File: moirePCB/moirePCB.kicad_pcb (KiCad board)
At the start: 4 copper layers, 30 x 228.8 mm, 37 parts, among them J1 USB_C_Receptacle, J2 Conn_01x12_Pin, SW3 SW_DPDT_x2, U1 ESP32-PICO-D4, U2 BQ24075RGT, U3 TLV73333PDBV, U4 RFM95W-915S2, U5 CH340E, U6 TLC555xD, U7 HDC1080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

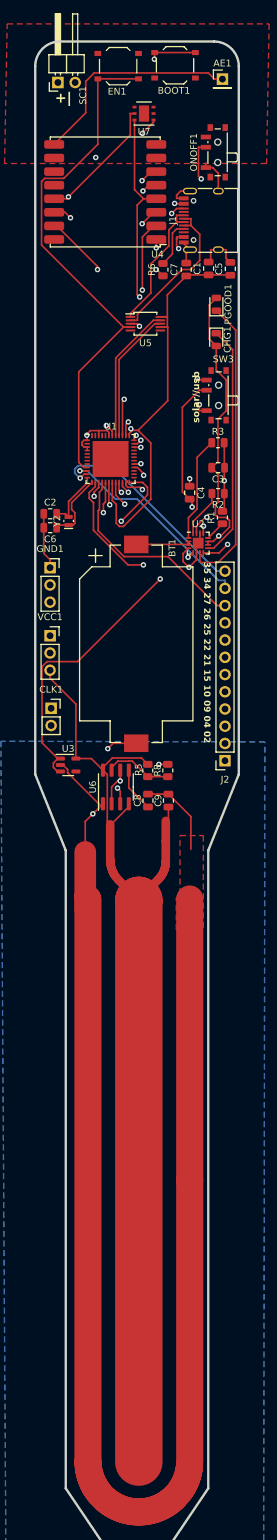
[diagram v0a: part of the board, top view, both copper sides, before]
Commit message: pins and jumpers, transistor A_RAIL
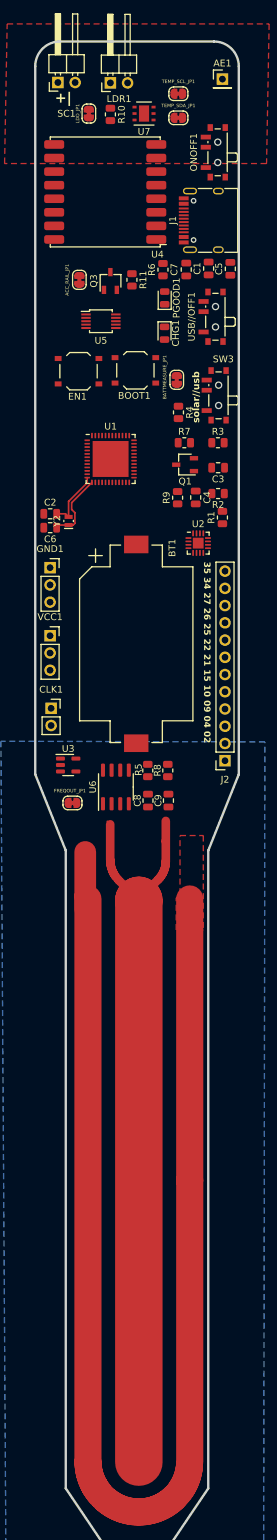
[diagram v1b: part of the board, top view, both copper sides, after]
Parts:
- added ACC_RAIL_JP1: SolderJumper_2_Bridged, Jumper:SolderJumper-2_P1.3mm_Bridged_RoundedPad1.0x1.5mm, F.Cu at (46.5, 46.9)
- added BATTMEASURE_JP1: SolderJumper_2_Bridged, Jumper:SolderJumper-2_P1.3mm_Bridged_RoundedPad1.0x1.5mm, F.Cu at (60.8, 61.6)
- added FREQOUT_JP1: SolderJumper_2_Bridged, Jumper:SolderJumper-2_P1.3mm_Bridged_RoundedPad1.0x1.5mm, F.Cu at (45.5, 124.0)
- added LDO_JP1: SolderJumper_2_Bridged, Jumper:SolderJumper-2_P1.3mm_Bridged_RoundedPad1.0x1.5mm, F.Cu at (47.9, 22.4)
- added LDR1: R_Photo 50k-100k, Connector_PinHeader_2.54mm:PinHeader_1x02_P2.54mm_Horizontal, F.Cu at (51.0, 17.8)
- added Q1: NPN, Package_TO_SOT_SMD:TSOT-23, F.Cu at (62.1, 74.1)
- added Q3: NPN, Package_TO_SOT_SMD:TSOT-23, F.Cu at (51.1, 47.0)
- added R10: 360k, Resistor_SMD:R_0805_2012Metric, F.Cu at (51.1, 22.5)
- added R11: 10k, Resistor_SMD:R_0805_2012Metric, F.Cu at (54.2, 46.9)
- added R4: 270k, Resistor_SMD:R_0805_2012Metric, F.Cu at (61.1, 66.4)
- added R7: 820k, Resistor_SMD:R_0805_2012Metric, F.Cu at (62.0, 70.9)
- added R9: 10k, Resistor_SMD:R_0805_2012Metric, F.Cu at (61.0, 79.0)
- added TEMP_SCL_JP1: SolderJumper_2_Bridged, Jumper:SolderJumper-2_P1.3mm_Bridged_RoundedPad1.0x1.5mm, F.Cu at (61.1, 19.4)
- added TEMP_SDA_JP1: SolderJumper_2_Bridged, Jumper:SolderJumper-2_P1.3mm_Bridged_RoundedPad1.0x1.5mm, F.Cu at (61.1, 23.0)
- added USB//OFF1: SW_DPDT_x2, Button_Switch_SMD:SW_SPDT_PCM12, F.Cu at (66.2, 52.3)
- moved BOOT1 45.3 mm to (54.7, 60.2)
- moved EN1 45.3 mm to (46.4, 60.3)
- moved CHG1 7.68 mm to (59.0, 54.7)
- moved PGOOD1 7.68 mm to (59.1, 49.5)
- moved U5 6.57 mm to (49.7, 53.0)
- moved C4 1.13 mm to (63.6, 78.9)
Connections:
- net /GPIO_25 renamed BATT_MEASURE
- C7 pad 1: VCC -> Net-(U5-V3)
- C9 pad 1: VCC -> A_VCC
- CLK1 pad 1: /GPIO_18 -> /GPIO_22
- J2 pad 11: /GPIO_34 -> FREQOUT
- R5 pad 2: VCC -> A_VCC
- U1 pad 10: /GPIO_34 -> FREQOUT
- U1 pad 15: FREQOUT -> ACCESSORY_SW
- U5 pad 10: VCC -> Net-(U5-V3)
- U5 pad 7: VCC -> Net-(U5-V3)
- U6 pad 3: FREQOUT -> Net-(FREQOUT_JP1-B)
- U6 pad 4: VCC -> A_VCC
- U6 pad 8: VCC -> A_VCC
- U7 pad 1: /GPIO_22 -> Net-(TEMP_SDA_JP1-A)
- U7 pad 5: VCC -> A_VCC
- U7 pad 6: /GPIO_18 -> Net-(TEMP_SCL_JP1-A)
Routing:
- net VCC: track 320.7 -> 110.1 mm, vias 3 -> 0
- net /GPIO_18: track 99.4 -> 0.00 mm, vias 2 -> 0
- net Net-(CHG1-A): track 95.6 -> 0.00 mm, vias 3 -> 0
- net GND: track 337.5 -> 247.1 mm, vias 9 -> 0
- net /EN: track 77.9 -> 0.00 mm
- net Net-(U1-IO0): track 74.7 -> 0.00 mm, vias 2 -> 0
- net Net-(SC1-+): track 62.2 -> 0.00 mm, vias 1 -> 0
- net /GPIO_14: track 59.6 -> 0.00 mm, vias 2 -> 0
- net Net-(ONOFF1A-B): track 59.3 -> 0.00 mm, vias 2 -> 0
- net /GPIO_13: track 52.0 -> 0.00 mm, vias 2 -> 0
- net FREQOUT: track 49.2 -> 0.00 mm, vias 2 -> 0
- net /GPIO_4: track 48.9 -> 0.00 mm, vias 1 -> 0
- net /GPIO_2: track 48.9 -> 0.00 mm, vias 1 -> 0
- net /GPIO_22: track 48.4 -> 0.00 mm, vias 2 -> 0
- net /GPIO_12: track 48.3 -> 0.00 mm, vias 2 -> 0
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
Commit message: pcb 2 final (submitted to jlc)
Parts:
- removed Q1, Q3: NPN, Package_TO_SOT_SMD:TSOT-23
- added EN2_JP1: SolderJumper_2_Bridged, Jumper:SolderJumper-2_P1.3mm_Bridged_RoundedPad1.0x1.5mm, F.Cu at (66.0, 90.9)
- added U8: AP2281-1WG-7, Package_TO_SOT_SMD:SOT-23-6, F.Cu at (62.0, 74.8)
- added U9: AP2281-1WG-7, Package_TO_SOT_SMD:SOT-23-6, F.Cu at (42.9, 67.0)
- J2: value Conn_01x12_Pin -> Conn_01x06_Socket; footprint Connector_PinSocket_2.54mm:PinSocket_1x12_P2.54mm_Vertical -> Connector_PinSocket_2.54mm:PinSocket_1x06_P2.54mm_Vertical
- R1: value 1.18k -> 7.5k
- R11, R9: value 10k -> 1k
- R2: value 1.13k -> 8.2
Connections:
- BT1 pad 1: Net-(BT1-+) -> VCC
- C3 pad 2: Net-(CHG1-A) -> Net-(U3-EN)
- J2 pad 6: /GPIO_21 -> /GPIO_27
- PGOOD1 pad 2: Net-(CHG1-A) -> Net-(PGOOD1-A)
- R11 pad 1: Net-(Q3-B) -> Net-(U3-EN)
- R11 pad 2: ACCESSORY_SW -> Net-(PGOOD1-A)
- R9 pad 1: Net-(Q1-B) -> Net-(U3-EN)
- R9 pad 2: ACCESSORY_SW -> Net-(CHG1-A)
- U1 pad 11: /GPIO_35 -> LDR_MEASURE
- U2 pad 10: Net-(CHG1-A) -> Net-(U3-EN)
- U2 pad 11: Net-(CHG1-A) -> Net-(U3-EN)
- U2 pad 2: Net-(BT1-+) -> VCC
- U2 pad 3: Net-(BT1-+) -> VCC
- U2 pad 5: Net-(CHG1-A) -> Net-(EN2_JP1-B)
- U3 pad 1: Net-(CHG1-A) -> Net-(U3-EN)
- U3 pad 3: Net-(CHG1-A) -> Net-(U3-EN)
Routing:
- net VCC: track 110.1 -> 342.9 mm, vias 0 -> 6
- net GND: track 247.1 -> 372.7 mm, vias 0 -> 22
- net A_VCC: track 0.00 -> 125.0 mm, vias 0 -> 2
- net Net-(U3-EN): track 0.00 -> 116.1 mm, vias 0 -> 5
- net /GPIO_22: track 0.00 -> 107.8 mm, vias 0 -> 3
- net /GPIO_18: track 0.00 -> 91.5 mm, vias 0 -> 2
- net Net-(SC1-+): track 0.00 -> 68.9 mm, vias 0 -> 1
- net /GPIO_14: track 0.00 -> 63.7 mm, vias 0 -> 2
- net Net-(ONOFF1A-B): track 0.00 -> 61.9 mm, vias 0 -> 2
- net /GPIO_13: track 0.00 -> 59.8 mm, vias 0 -> 2
- net LDR_MEASURE: track 0.00 -> 55.9 mm, vias 0 -> 2
- net FREQOUT: track 0.00 -> 54.8 mm
- net /GPIO_21: track 0.00 -> 53.3 mm, vias 0 -> 2
- net /GPIO_12: track 0.00 -> 49.2 mm, vias 0 -> 2
- net /GPIO_2: track 0.00 -> 47.9 mm, vias 0 -> 2
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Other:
- board text added: "2 4 9 10 15 27"
- board text removed: "35 34 27 26 25 22 21 15 10 09 04 02"

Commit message: initial pcb 3 layout
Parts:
- added C3: .01uF, Capacitor_SMD:C_0805_2012Metric, F.Cu at (57.8, 101.4)
- added C_FLTR1: .1uF, Capacitor_SMD:C_0805_2012Metric, F.Cu at (57.8, 104.4)
- added C_HVR1: 4.7uF, Capacitor_SMD:C_0805_2012Metric, F.Cu at (57.8, 107.4)
- added C_STOR1: 4.7uF, Capacitor_SMD:C_0805_2012Metric, F.Cu at (57.8, 110.4)
- added L_BST1: 22uH, Inductor_SMD:L_0805_2012Metric, F.Cu at (61.2, 97.7)
- added R_OC_1: R, Resistor_SMD:R_0805_2012Metric, F.Cu at (47.9, 92.5)
- added R_OC_2: R, Resistor_SMD:R_0805_2012Metric, F.Cu at (47.9, 95.4)
- added R_OK_1: R, Resistor_SMD:R_0805_2012Metric, F.Cu at (47.9, 98.4)
- added R_OK_2: R, Resistor_SMD:R_0805_2012Metric, F.Cu at (52.3, 92.5)
- added R_OK_3: R, Resistor_SMD:R_0805_2012Metric, F.Cu at (52.3, 95.4)
- added R_OV_1: R, Resistor_SMD:R_0805_2012Metric, F.Cu at (52.3, 98.4)
- added R_OV_2: R, Resistor_SMD:R_0805_2012Metric, F.Cu at (56.8, 92.5)
- added R_UV_1: R, Resistor_SMD:R_0805_2012Metric, F.Cu at (56.8, 95.4)
- added R_UV_2: R, Resistor_SMD:R_0805_2012Metric, F.Cu at (56.8, 98.4)
- added U10: TLV73333PDBV, Package_TO_SOT_SMD:SOT-23-5, F.Cu at (62.6, 106.5)
- added U2: BQ25504, Package_DFN_QFN:VQFN-16-1EP_3x3mm_P0.5mm_EP1.68x1.68mm, F.Cu at (61.6, 93.7)
- added U3: TLV73333PDBV, Package_TO_SOT_SMD:SOT-23-5, F.Cu at (62.6, 102.1)
- added USB//SOLAR1: SW_DPDT_x2, Button_Switch_SMD:SW_SPDT_PCM12, F.Cu at (50.6, 102.8)
- BT1: footprint Battery:BatteryHolder_Keystone_1060_1x2032 -> Connector_JST:JST_EH_S2B-EH_1x02_P2.50mm_Horizontal
- moved BT1 11.9 mm to (47.6, 110.0)
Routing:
- net VCC: track 342.9 -> 110.1 mm, vias 6 -> 0
- net GND: track 372.7 -> 247.1 mm, vias 22 -> 0
- net A_VCC: track 125.0 -> 0.00 mm, vias 2 -> 0
- net Net-(U3-EN): track 116.1 -> 0.00 mm, vias 5 -> 0
- net /GPIO_22: track 107.8 -> 0.00 mm, vias 3 -> 0
- net /GPIO_18: track 91.5 -> 0.00 mm, vias 2 -> 0
- net Net-(SC1-+): track 68.9 -> 0.00 mm, vias 1 -> 0
- net /GPIO_14: track 63.7 -> 0.00 mm, vias 2 -> 0
- net Net-(ONOFF1A-B): track 61.9 -> 0.00 mm, vias 2 -> 0
- net /GPIO_13: track 59.8 -> 0.00 mm, vias 2 -> 0
- net LDR_MEASURE: track 55.9 -> 0.00 mm, vias 2 -> 0
- net FREQOUT: track 54.8 -> 0.00 mm
- net /GPIO_21: track 53.3 -> 0.00 mm, vias 2 -> 0
- net /GPIO_12: track 49.2 -> 0.00 mm, vias 2 -> 0
- net /GPIO_2: track 47.9 -> 0.00 mm, vias 2 -> 0
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
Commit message: r values needed
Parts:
- moved U9 21.9 mm to (56.4, 84.3)
- moved USB//SOLAR1 17.9 mm to (67.7, 97.7), turned to 90 degrees
- moved R6 12.6 mm to (61.0, 57.8), turned to 180 degrees
- moved ACC_RAIL_JP1 12.4 mm to (56.3, 54.5)
- moved LDO_JP1 12.3 mm to (57.5, 14.7)
- moved U7 9.40 mm to (61.3, 14.6)
- moved R10 8.38 mm to (59.3, 21.0)
- moved LDR1 6.90 mm to (50.8, 24.7)
- moved SC1 6.90 mm to (43.1, 24.7)
- moved TEMP_SDA_JP1 6.28 mm to (67.1, 21.1), turned to 90 degrees
- moved R11 4.08 mm to (56.3, 50.4)
- moved C3 3.05 mm to (57.4, 104.4)
- moved C_FLTR1 3.05 mm to (57.4, 107.4)
- moved C_HVR1 3.05 mm to (57.4, 110.4)
- moved C_STOR1 3.05 mm to (57.4, 113.4)
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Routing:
- net VCC: track 110.1 -> 0.00 mm
- net FREQOUT: track 0.00 -> 110.1 mm

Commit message: pre route
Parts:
- removed the C3 at (66.9, 74.5)
- removed C4: 1u, Capacitor_SMD:C_0805_2012Metric
- removed CHG1, PGOOD1: LED, LED_SMD:LED_0805_2012Metric
- removed R1: 7.5k, Resistor_SMD:R_0805_2012Metric
- removed R11, R9: 1k, Resistor_SMD:R_0805_2012Metric
- removed R2: 8.2, Resistor_SMD:R_0805_2012Metric
- removed R3: 10k, Resistor_SMD:R_0805_2012Metric
- removed the U2 at (64.0, 85.7)
- added VBAT_OK1: SolderJumper_2_Bridged, Jumper:SolderJumper-2_P1.3mm_Bridged_RoundedPad1.0x1.5mm, F.Cu at (62.2, 91.1)
- moved ACC_RAIL_JP1 26.1 mm to (66.7, 78.3), turned to 0 degrees
- moved R6 23.3 mm to (62.3, 81.0), turned to 0 degrees
- moved BATTMEASURE_JP1 21.1 mm to (66.7, 81.9), turned to 0 degrees
- moved U9 15.9 mm to (66.7, 72.1)
- moved BT1 15.2 mm to (48.6, 95.6)
- moved R_OC_1 14.8 mm to (48.1, 107.2)
- moved R_OC_2 14.8 mm to (48.1, 110.2)
- moved R_OK_1 14.8 mm to (48.1, 113.2)
- moved R_OK_2 14.8 mm to (52.5, 107.2)
- moved R_OK_3 14.8 mm to (52.5, 110.2)
- moved R_OV_1 14.8 mm to (52.5, 113.2)
- moved U2 14.2 mm to (49.8, 101.5)
- moved R7 13.1 mm to (62.3, 84.0)
- moved U8 11.9 mm to (66.6, 85.8)
- moved R4 11.7 mm to (62.3, 78.0), turned to 0 degrees
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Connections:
- BT1 pad 1: VCC -> Net-(BT1-+)
- U10 pad 3: VBAT_OK -> Net-(U10-EN)
- U2 pad 14: VCC -> Net-(BT1-+)
- U8 pad 4: VCC -> Net-(BT1-+)
- U8 pad 6: VCC -> Net-(BT1-+)

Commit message: resistorValues
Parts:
- added R_OC+10: 10M, Resistor_SMD:R_0805_2012Metric, F.Cu at (61.8, 113.5)
- R_OC_1: value R -> 5.76M
- R_OC_2: value R -> 4.12M
- R_OK_1: value R -> 3.57M
- R_OK_2, R_UV_2: value R -> 6.19M
- R_OK_3: value R -> .143M
- R_OV_1: value R -> 4.42M
- R_OV_2: value R -> 5.36M
- R_UV_1: value R -> 3.74M
- moved U3 0.37 mm to (62.2, 105.0)
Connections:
- L_BST1 pad 1: Net-(SC1-+) -> Net-(U2-VIN_DC)
- R_OC_2 pad 2: Net-(U2-VOC_SAMP) -> Net-(R_OC+10-Pad1)
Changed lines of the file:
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@@
   (net 94 "Net-(BT1-+)")
   (net 95 "Net-(U10-EN)")
+  (net 96 "Net-(R_OC+10-Pad1)")
   (footprint "Connector_PinSocket_2.54mm:PinSocket_1x06_P2.54mm_Vertical" (layer "F.Cu")
     (at 67.945 117.729 180)
@@
       (stroke (width 0.1) (type solid)) (layer "F.Fab"))
     (pad "1" smd roundrect (at -1.0625 0) (size 0.875 1.2) (layers "F.Cu" "F.Paste" "F.Mask") (roundrect_rratio 0.25)
-      (net 40 "Net-(SC1-+)") (pinfunction "1") (pintype "passive"))
+      (net 85 "Net-(U2-VIN_DC)") (pinfunction "1") (pintype "passive"))
     (pad "2" smd roundrect (at 1.0625 0) (size 0.875 1.2) (layers "F.Cu" "F.Paste" "F.Mask") (roundrect_rratio 0.25)
       (net 83 "Net-(U2-LBST)") (pinfunction "2") (pintype "passive"))
@@
         (effects (font (size 1 1) (thickness 0.15)))
     )
-    (fp_text value "R" (at 0 1.65) (layer "F.Fab")
+    (fp_text value "6.19M" (at 0 1.65) (layer "F.Fab")
         (effects (font (size 1 1) (thickness 0.15)))
     )
@@
         (effects (font (size 1 1) (thickness 0.15)))
     )
-    (fp_text value "R" (at 0 1.65) (layer "F.Fab")
+    (fp_text value "3.57M" (at 0 1.65) (layer "F.Fab")
         (effects (font (size 1 1) (thickness 0.15)))
     )
@@
         (effects (font (size 1 1) (thickness 0.15)))
     )
-    (fp_text value "R" (at 0 1.65) (layer "F.Fab")
+    (fp_text value "5.36M" (at 0 1.65) (layer "F.Fab")
         (effects (font (size 1 1) (thickness 0.15)))
     )
@@
         (effects (font (size 1 1) (thickness 0.15)))
     )
-    (fp_text value "R" (at 0 1.65) (layer "F.Fab")
+    (fp_text value "4.42M" (at 0 1.65) (layer "F.Fab")
         (effects (font (size 1 1) (thickness 0.15)))
     )
@@
         (effects (font (size 1 1) (thickness 0.15)))
     )
-    (fp_text value "R" (at 0 1.65) (layer "F.Fab")
+    (fp_text value "5.76M" (at 0 1.65) (layer "F.Fab")
         (effects (font (size 1 1) (thickness 0.15)))
     )
@@
   )
   (footprint "Package_TO_SOT_SMD:SOT-23-5" (layer "F.Cu")
-    (at 61.834 105.005)
+    (at 62.2 105.005)
     (descr "SOT, 5 Pin (https://www.jedec.org/sites/default/files/docs/Mo-178c.PDF variant AA), generated with kicad-footprint-generator ipc_gullwing_generator.py")
     (tags "SOT TO_SOT_SMD")
@@
       ))
   )
+  (footprint "Resistor_SMD:R_0805_2012Metric" (layer "F.Cu")
+    (at 61.8125 113.45 180)
+    (descr "Resistor SMD 0805 (2012 Metric), square (rectangular) end terminal, IPC_7351 nominal, (Body size source: IPC-SM-782 page 72, https://www.pcb-3d.com/wordpress/wp-content/uploads/ipc-sm-782a_amendment_1_and_2.pdf), generated with kicad-footprint-generator")
+    (tags "resistor")
+    (property "Sheetfile" "moirePCB.kicad_sch")
+    (property "Sheetname" "")
+    (property "ki_description" "Resistor")
+    (property "ki_keywords" "R res resistor")
+    (attr smd)
+    (fp_text reference "R_OC+10" (at 0 -1.65) (layer "F.SilkS")
+        (effects (font (size 1 1) (thickness 0.15)))
+    )
+    (fp_text value "10M" (at 0 1.65) (layer "F.Fab")
+        (effects (font (size 1 1) (thickness 0.15)))
+    )
+    (fp_text user "${REFERENCE}" (at 0 0) (layer "F.Fab")
+        (effects (font (size 0.5 0.5) (thickness 0.08)))
+    )
+    (fp_line (start -0.227064 -0.735) (end 0.227064 -0.735)
+      (stroke (width 0.12) (type solid)) (layer "F.SilkS"))
+    (fp_line (start -0.227064 0.735) (end 0.227064 0.735)
+      (stroke (width 0.12) (type solid)) (layer "F.SilkS"))
+    (fp_line (start -1.68 -0.95) (end 1.68 -0.95)
+      (stroke (width 0.05) (type solid)) (layer "F.CrtYd"))
+    (fp_line (start -1.68 0.95) (end -1.68 -0.95)
+      (stroke (width 0.05) (type solid)) (layer "F.CrtYd"))
+    (fp_line (start 1.68 -0.95) (end 1.68 0.95)
+      (stroke (width 0.05) (type solid)) (layer "F.CrtYd"))
+    (fp_line (start 1.68 0.95) (end -1.68 0.95)
+      (stroke (width 0.05) (type solid)) (layer "F.CrtYd"))
+    (fp_line (start -1 -0.625) (end 1 -0.625)
+      (stroke (width 0.1) (type solid)) (layer "F.Fab"))
+    (fp_line (start -1 0.625) (end -1 -0.625)
+      (stroke (width 0.1) (type solid)) (layer "F.Fab"))
+    (fp_line (start 1 -0.625) (end 1 0.625)
+      (stroke (width 0.1) (type solid)) (layer "F.Fab"))
+    (fp_line (start 1 0.625) (end -1 0.625)
+      (stroke (width 0.1) (type solid)) (layer "F.Fab"))
+    (pad "1" smd roundrect (at -0.9125 0 180) (size 1.025 1.4) (layers "F.Cu" "F.Paste" "F.Mask") (roundrect_rratio 0.243902)
+      (net 96 "Net-(R_OC+10-Pad1)") (pintype "passive"))
+    (pad "2" smd roundrect (at 0.9125 0 180) (size 1.025 1.4) (layers "F.Cu" "F.Paste" "F.Mask") (roundrect_rratio 0.243902)
+      (net 84 "Net-(U2-VOC_SAMP)") (pintype "passive"))
+    (model "${KICAD6_3DMODEL_DIR}/Resistor_SMD.3dshapes/R_0805_2012Metric.wrl"
+      (offset (xyz 0 0 0))
+      (scale (xyz 1 1 1))
+      (rotate (xyz 0 0 0))
+    )
+  )
   (footprint "Button_Switch_SMD:SW_Push_1P1T_XKB_TS-1187A" (layer "F.Cu")
     (at 46.355 60.325)
@@
         (effects (font (size 1 1) (thickness 0.15)))
     )
-    (fp_text value "R" (at -0.396 4.674) (layer "F.Fab")
+    (fp_text value "6.19M" (at -0.396 4.674) (layer "F.Fab")
         (effects (font (size 1 1) (thickness 0.15)))
     )
@@
         (effects (font (size 1 1) (thickness 0.15)))
     )
-    (fp_text value "R" (at 0 1.65) (layer "F.Fab")
+    (fp_text value "3.74M" (at 0 1.65) (layer "F.Fab")
         (effects (font (size 1 1) (thickness 0.15)))
     )
@@
         (effects (font (size 1 1) (thickness 0.15)))
     )
-    (fp_text value "R" (at 0 1.65) (layer "F.Fab")
+    (fp_text value ".143M" (at 0 1.65) (layer "F.Fab")
         (effects (font (size 1 1) (thickness 0.15)))
     )
@@
         (effects (font (size 1 1) (thickness 0.15)))
     )
-    (fp_text value "R" (at 0 1.65) (layer "F.Fab")
+    (fp_text value "4.12M" (at 0 1.65) (layer "F.Fab")
         (effects (font (size 1 1) (thickness 0.15)))
     )
@@
       (net 85 "Net-(U2-VIN_DC)") (pintype "passive"))
     (pad "2" smd roundrect (at 0.9125 0) (size 1.025 1.4) (layers "F.Cu" "F.Paste" "F.Mask") (roundrect_rratio 0.243902)
-      (net 84 "Net-(U2-VOC_SAMP)") (pintype "passive"))
+      (net 96 "Net-(R_OC+10-Pad1)") (pintype "passive"))
     (model "${KICAD6_3DMODEL_DIR}/Resistor_SMD.3dshapes/R_0805_2012Metric.wrl"
       (offset (xyz 0 0 0))

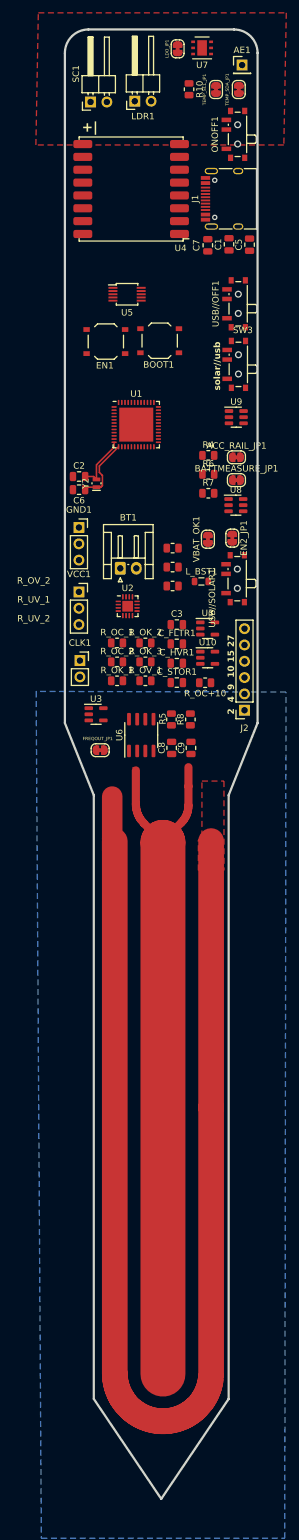
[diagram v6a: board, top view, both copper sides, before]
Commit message: hole battery outline
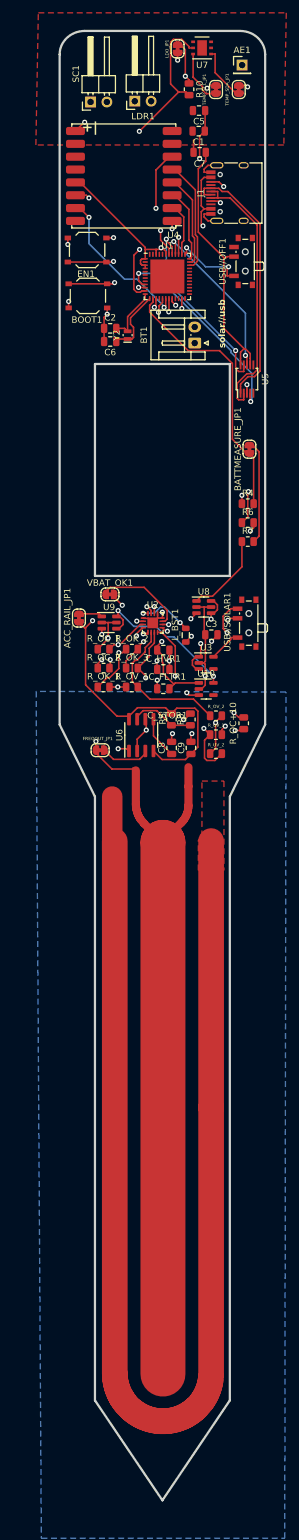
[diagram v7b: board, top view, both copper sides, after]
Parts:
- removed CLK1: Conn_01x02_Pin, Connector_PinSocket_2.54mm:PinSocket_1x02_P2.54mm_Vertical
- removed EN2_JP1: SolderJumper_2_Bridged, Jumper:SolderJumper-2_P1.3mm_Bridged_RoundedPad1.0x1.5mm
- removed GND1, VCC1: Conn_01x03_Pin, Connector_PinSocket_2.54mm:PinSocket_1x03_P2.54mm_Vertical
- removed J2: Conn_01x06_Socket, Connector_PinSocket_2.54mm:PinSocket_1x06_P2.54mm_Vertical
- removed ONOFF1, SW3: SW_DPDT_x2, Button_Switch_SMD:SW_SPDT_PCM12
- removed the U3 at (44.8, 118.4)
- moved U9 37.6 mm to (46.9, 104.1)
- moved BT1 36.9 mm to (60.2, 60.6), turned to 90 degrees
- moved ACC_RAIL_JP1 35.0 mm to (42.2, 103.4), turned to 90 degrees
- moved R_OV_2 27.0 mm to (63.5, 118.6)
- moved R_UV_1 27.0 mm to (63.5, 121.5)
- moved R_UV_2 27.0 mm to (63.5, 124.5)
- moved U1 23.6 mm to (55.9, 50.2)
- moved Y2 23.6 mm to (49.7, 59.3)
- moved C2 23.6 mm to (47.0, 58.3)
- moved C6 23.6 mm to (47.0, 60.3)
- moved U5 22.9 mm to (68.3, 66.2), turned to 90 degrees
- moved C5 22.3 mm to (60.9, 24.4), turned to 180 degrees
- moved C1 18.2 mm to (60.8, 27.6), turned to 180 degrees
- moved VBAT_OK1 17.5 mm to (47.0, 99.7), turned to 0 degrees
- moved U8 16.6 mm to (61.6, 101.7)
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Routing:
- net VCC: track 0.00 -> 153.8 mm, vias 0 -> 7
- net A_VCC: track 0.00 -> 149.5 mm, vias 0 -> 2
- net Net-(SC1-+): track 0.00 -> 133.6 mm, vias 0 -> 2
- net /USB5V: track 0.00 -> 86.0 mm, vias 0 -> 2
- net FREQOUT: track 110.1 -> 194.6 mm, vias 0 -> 2
- net ACCESSORY_SW: track 0.00 -> 74.2 mm, vias 0 -> 3
- net GND: track 247.1 -> 313.3 mm, vias 0 -> 18
- net Net-(BT1-+): track 0.00 -> 62.1 mm, vias 0 -> 2
- net Net-(J1-CC2): track 0.00 -> 56.6 mm, vias 0 -> 2
- net Net-(J1-CC1): track 0.00 -> 56.5 mm, vias 0 -> 2
- net /EN: track 0.00 -> 44.3 mm, vias 0 -> 3
- net LDR_MEASURE: track 0.00 -> 43.3 mm, vias 0 -> 2
- net /D-: track 0.00 -> 42.0 mm
- net BATT_MEASURE: track 0.00 -> 42.0 mm
- net Net-(U5-V3): track 0.00 -> 41.5 mm
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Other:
- board size 30 x 228.8 mm -> 32 x 228.8 mm
- board text removed: "2 4 9 10 15 27"
